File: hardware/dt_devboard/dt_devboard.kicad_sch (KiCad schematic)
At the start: 1 part

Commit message: added hieracrchial sheet structure on schematic
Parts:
- removed IC?: STM32WB35CEU6A, QFN50P700X700X60-49N-D, symbol SamacSys_Parts:STM32WB35CEU6A
- added IC?: MIMXRT1015CAF4A, QFP50P1600X1600X170-100N, symbol MIMXRT1015CAF4A:MIMXRT1015CAF4A
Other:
- added sheet Power (power_subsystem.kicad_sch)
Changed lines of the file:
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@@
 (kicad_sch (version 20211123) (generator eeschema)
-  (paper "A4")
-  (symbol (lib_id "SamacSys_Parts:STM32WB35CEU6A") (at 44.45 45.72 0) (unit 1)
+  (paper "A2")
+  (symbol (lib_id "MIMXRT1015CAF4A:MIMXRT1015CAF4A") (at 49.53 57.15 0) (unit 1)
     (in_bom yes) (on_board yes) (fields_autoplaced)
-    (property "Reference" "IC?" (id 0) (at 95.25 39.1412 0))
-    (property "Value" "STM32WB35CEU6A" (id 1) (at 95.25 41.6812 0))
-    (property "Footprint" "QFN50P700X700X60-49N-D" (id 2) (at 86.36 33.02 0)
+    (property "Reference" "IC?" (id 0) (at 130.81 50.5712 0))
+    (property "Value" "MIMXRT1015CAF4A" (id 1) (at 130.81 53.1112 0))
+    (property "Footprint" "QFP50P1600X1600X170-100N" (id 2) (at 121.92 34.29 0)
       (effects (font (size 1.27 1.27)) (justify left) hide)
     )
-    (property "Datasheet" "https://componentsearchengine.com/Datasheets/2/STM32WB35CEU6A.pdf" (id 3) (at 86.36 35.56 0)
+    (property "Datasheet" "http://www.nxp.com/docs/en/data-sheet/IMXRT1015IEC.pdf" (id 3) (at 121.92 36.83 0)
       (effects (font (size 1.27 1.27)) (justify left) hide)
     )
-    (property "Description" "ARM Microcontrollers - MCU 16/32-BITS MICROS" (id 4) (at 86.36 38.1 0)
+    (property "Description" "ARM Microcontrollers - MCU i.MXRT1015, 100LQFP" (id 4) (at 121.92 39.37 0)
       (effects (font (size 1.27 1.27)) (justify left) hide)
     )
-    (property "Height" "0.6" (id 5) (at 86.36 40.64 0)
+    (property "Height" "1.7" (id 5) (at 121.92 41.91 0)
       (effects (font (size 1.27 1.27)) (justify left) hide)
     )
-    (property "Manufacturer_Name" "STMicroelectronics" (id 6) (at 86.36 43.18 0)
+    (property "Manufacturer_Name" "NXP" (id 6) (at 121.92 44.45 0)
       (effects (font (size 1.27 1.27)) (justify left) hide)
     )
-    (property "Manufacturer_Part_Number" "STM32WB35CEU6A" (id 7) (at 86.36 45.72 0)
+    (property "Manufacturer_Part_Number" "MIMXRT1015CAF4A" (id 7) (at 121.92 46.99 0)
       (effects (font (size 1.27 1.27)) (justify left) hide)
     )
-    (property "Mouser Part Number" "511-STM32WB35CEU6A" (id 8) (at 86.36 48.26 0)
+    (property "Mouser Part Number" "771-MIMXRT1015CAF4A" (id 8) (at 121.92 49.53 0)
       (effects (font (size 1.27 1.27)) (justify left) hide)
     )
-    (property "Mouser Price/Stock" "https://www.mouser.co.uk/ProductDetail/STMicroelectronics/STM32WB35CEU6A?qs=DPoM0jnrROX%252BdiHaOx6y1Q%3D%3D" (id 9) (at 86.36 50.8 0)
+    (property "Mouser Price/Stock" "https://www.mouser.co.uk/ProductDetail/NXP-Semiconductors/MIMXRT1015CAF4A?qs=l7cgNqFNU1janL%2F6ip864Q%3D%3D" (id 9) (at 121.92 52.07 0)
       (effects (font (size 1.27 1.27)) (justify left) hide)
     )
-    (property "Arrow Part Number" "STM32WB35CEU6A" (id 10) (at 86.36 53.34 0)
+    (property "Arrow Part Number" "" (id 10) (at 121.92 54.61 0)
       (effects (font (size 1.27 1.27)) (justify left) hide)
     )
-    (property "Arrow Price/Stock" "https://www.arrow.com/en/products/stm32wb35ceu6a/stmicroelectronics?region=nac" (id 11) (at 86.36 55.88 0)
+    (property "Arrow Price/Stock" "" (id 11) (at 121.92 57.15 0)
       (effects (font (size 1.27 1.27)) (justify left) hide)
     )
     (pin "1")
     (pin "10")
+    (pin "100")
     (pin "11")
     (pin "12")
@@
     (pin "49")
     (pin "5")
+    (pin "50")
+    (pin "51")
+    (pin "52")
+    (pin "53")
+    (pin "54")
+    (pin "55")
+    (pin "56")
+    (pin "57")
+    (pin "58")
+    (pin "59")
     (pin "6")
+    (pin "60")
+    (pin "61")
+    (pin "62")
+    (pin "63")
+    (pin "64")
+    (pin "65")
+    (pin "66")
+    (pin "67")
+    (pin "68")
+    (pin "69")
     (pin "7")
+    (pin "70")
+    (pin "71")
+    (pin "72")
+    (pin "73")
+    (pin "74")
+    (pin "75")
+    (pin "76")
+    (pin "77")
+    (pin "78")
+    (pin "79")
     (pin "8")
+    (pin "80")
+    (pin "81")
+    (pin "82")
+    (pin "83")
+    (pin "84")
+    (pin "85")
+    (pin "86")
+    (pin "87")
+    (pin "88")
+    (pin "89")
     (pin "9")
+    (pin "90")
+    (pin "91")
+    (pin "92")
+    (pin "93")
+    (pin "94")
+    (pin "95")
+    (pin "96")
+    (pin "97")
+    (pin "98")
+    (pin "99")
+  )
+  (sheet (at 491.49 58.42) (size 50.8 71.12) (fields_autoplaced)
+    (stroke (width 0.1524) (type solid) (color 0 0 0 0))
+    (fill (color 0 0 0 0.0000))
+    (property "Sheet name" "Power" (id 0) (at 491.49 57.7084 0)
+      (effects (font (size 1.27 1.27)) (justify left bottom))
+    )
+    (property "Sheet file" "power_subsystem.kicad_sch" (id 1) (at 491.49 130.1246 0)
+      (effects (font (size 1.27 1.27)) (justify left top))
+    )
   )
   (sheet_instances
     (path "/" (page "1"))
+    (path "/6fe27d7a-8728-4218-b48e-6f66377c607f" (page "2"))
   )
   (symbol_instances
-    (path "/403cca15-d759-4eca-91db-c121522189fc"
-      (reference "IC?") (unit 1) (value "STM32WB35CEU6A") (footprint "QFN50P700X700X60-49N-D")
+    (path "/a108bf74-3a91-4c0a-8c67-2d89e262b919"
+      (reference "IC?") (unit 1) (value "MIMXRT1015CAF4A") (footprint "QFP50P1600X1600X170-100N")
+    )
+    (path "/6fe27d7a-8728-4218-b48e-6f66377c607f/38cad123-e6f8-46ac-bb65-7bf207c8a5a7"
+      (reference "J?") (unit 1) (value "UJ31-CH-G1-SMT-TR") (footprint "CUI_UJ31-CH-G1-SMT-TR")
     )
   )

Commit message: added USB signals to MCU
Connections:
- net USB_DN1: now reaches IC?.41 (USB_OTG1_DN)
- net USB_DP1: now reaches IC?.42 (USB_OTG1_DP)
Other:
- sheet Power ports: added USB_DN1, USB_DN2, USB_DP1, USB_DP2; removed none
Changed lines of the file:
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@@
 (kicad_sch (version 20211123) (generator eeschema)
   (paper "A2")
+  (wire (pts (xy 95.25 146.05) (xy 95.25 151.13))
+    (stroke (width 0) (type default) (color 0 0 0 0))
+  )
+  (wire (pts (xy 97.79 146.05) (xy 97.79 151.13))
+    (stroke (width 0) (type default) (color 0 0 0 0))
+  )
+  (hierarchical_label "USB_DP1" (shape input) (at 97.79 151.13 270)
+    (effects (font (size 1.27 1.27)) (justify right))
+  )
+  (hierarchical_label "USB_DN1" (shape input) (at 95.25 151.13 270)
+    (effects (font (size 1.27 1.27)) (justify right))
+  )
   (symbol (lib_id "MIMXRT1015CAF4A:MIMXRT1015CAF4A") (at 49.53 57.15 0) (unit 1)
     (in_bom yes) (on_board yes) (fields_autoplaced)
@@
       (effects (font (size 1.27 1.27)) (justify left top))
     )
+    (pin "USB_DP2" output (at 491.49 69.85 180)
+      (effects (font (size 1.27 1.27)) (justify left))
+    )
+    (pin "USB_DP1" output (at 491.49 74.93 180)
+      (effects (font (size 1.27 1.27)) (justify left))
+    )
+    (pin "USB_DN1" output (at 491.49 80.01 180)
+      (effects (font (size 1.27 1.27)) (justify left))
+    )
+    (pin "USB_DN2" output (at 491.49 85.09 180)
+      (effects (font (size 1.27 1.27)) (justify left))
+    )
   )
   (sheet_instances
@@
   )
   (symbol_instances
+    (path "/6fe27d7a-8728-4218-b48e-6f66377c607f/31cac15e-bcad-4ac1-ba6d-6a7d3365c9db"
+      (reference "#PWR?") (unit 1) (value "VBUS") (footprint "")
+    )
+    (path "/6fe27d7a-8728-4218-b48e-6f66377c607f/5a889284-4c9f-49be-8f02-e43e18550914"
+      (reference "#PWR?") (unit 1) (value "GND") (footprint "")
+    )
+    (path "/6fe27d7a-8728-4218-b48e-6f66377c607f/60b6fd94-83fa-4737-bac1-4732bb229ea8"
+      (reference "D?") (unit 1) (value "SML-D12M1WT86") (footprint "LED_SML-D12M1WT86")
+    )
     (path "/a108bf74-3a91-4c0a-8c67-2d89e262b919"
       (reference "IC?") (unit 1) (value "MIMXRT1015CAF4A") (footprint "QFP50P1600X1600X170-100N")

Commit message: added schematic sheets, symbols, and esp32 design
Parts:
- added C1: 10uF, symbol Device:C
- added C10, C11: TBD, symbol Device:C
- added C12, C13, C14, C2, C6: 0.1uF, symbol Device:C
- added C3, C5, C7, C8, C9: NC, symbol Device:C
- added C4: 1uF, symbol Device:C
- added IC2: ESP32-C3, QFN50P500X500X90-33N-D, symbol SamacSys_Parts:ESP32-C3
- added L1: TBD, symbol Device:L
- added L2: 2.0nH, symbol Device:L
- added PCBANT1: ANT1, symbol Custom:ANT1
- added R1: 0, symbol Device:R_US
- added R2: 499, symbol Device:R_US
- added Y1: Crystal_GND24, symbol Device:Crystal_GND24
- gave numbers to parts that had none: 1
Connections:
- new net: C11.2, IC2.29 (XTAL_N), Y1.3
- new net: C2.1, L1.1, PCBANT1. (LNA_OUT)
- new net: C5.1, IC2.1 (LNA_IN), L1.2
- new net: C10.2, R1.1, Y1.1
- new net: IC2.30 (XTAL_P), R1.2
- new net: C7.1, IC2.2 (VDD3P3_1), IC2.3 (VDD3P3_2), L2.2
- new net: IC2.28 (U0TXD), R2.2
- new net +3V3: C1.1, C12.1, C13.1, C14.1, C3.1, C4.1, C6.1, C8.1, C9.1, IC2.11 (VDD3P3_RTC), IC2.17 (VDD3P3_CPU), IC2.18 (VDD_SPI), IC2.31 (VDDA_1), IC2.32 (VDDA_2), L2.1
- new net CHIP_EN: IC2.7 (CHIP_EN)
- new net GND: C1.2, C10.1, C11.1, C12.2, C13.2, C14.2, C2.2, C3.2, C4.2, C5.2, C6.2, C7.2, C8.2, C9.2, IC2.33 (GND), PCBANT1. (LNA_OUT), Y1.2, Y1.4
- new net GPIO0: IC2.4 (XTAL_32K_P)
- new net GPIO1: IC2.5 (XTAL_32K_N)
- new net GPIO10: IC2.16 (GPIO10)
- new net GPIO12: IC2.19 (SPIHD)
- new net GPIO13: IC2.20 (SPIWP)
- new net GPIO18/USB_D-: IC2.25 (GPIO18)
- new net GPIO19/USB_D+: IC2.26 (GPIO19)
- new net GPIO2: IC2.6 (GPIO2)
- new net GPIO3: IC2.8 (GPIO3)
- new net GPIO8: IC2.14 (GPIO8)
- new net GPIO9: IC2.15 (GPIO9)
- new net MTDI: IC2.10 (MTDI)
- new net MTMS: IC2.9 (MTMS)
- new net SPICLK: IC2.22 (SPICLK)
- new net SPICS0: IC2.21 (SPICS0)
- new net SPID: IC2.23 (SPID)
- new net SPIQ: IC2.24 (SPIQ)
- new net U0RXD: IC2.27 (U0RXD)
- new net U0TXD: R2.1
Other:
- sheet Power renamed usb_subsystem
- added sheet external_clocks (external_clocks_sch.kicad_sch)
- added sheet external_memory (external_memory.kicad_sch)
- sheet usb_subsystem: file power_subsystem.kicad_sch -> usb_subsystem.kicad_sch
- note added: "32K crystal"
- note added: "ESP32"
- note added: "MCU"
- moved on the sheet: IC1

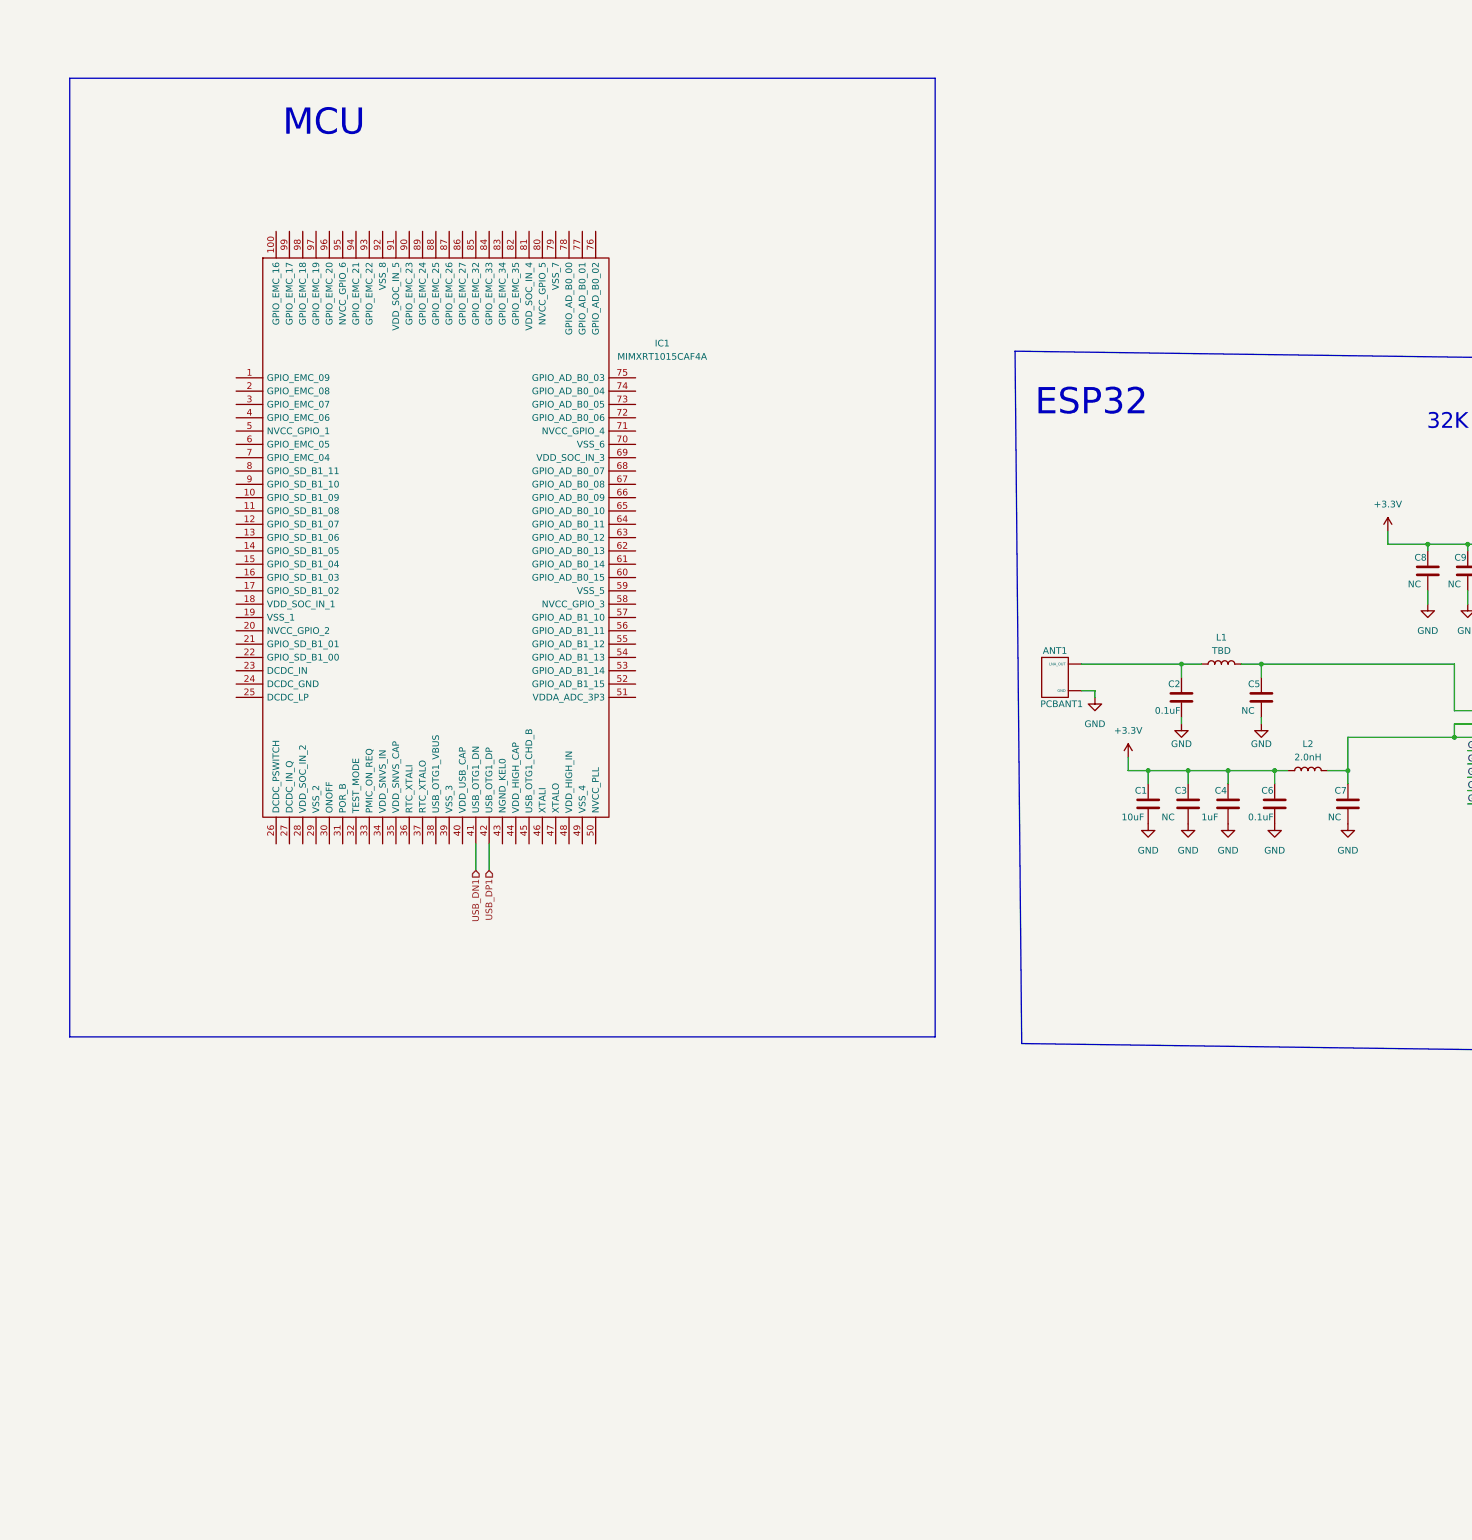
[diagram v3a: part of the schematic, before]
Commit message: added JTAG and SD connectors
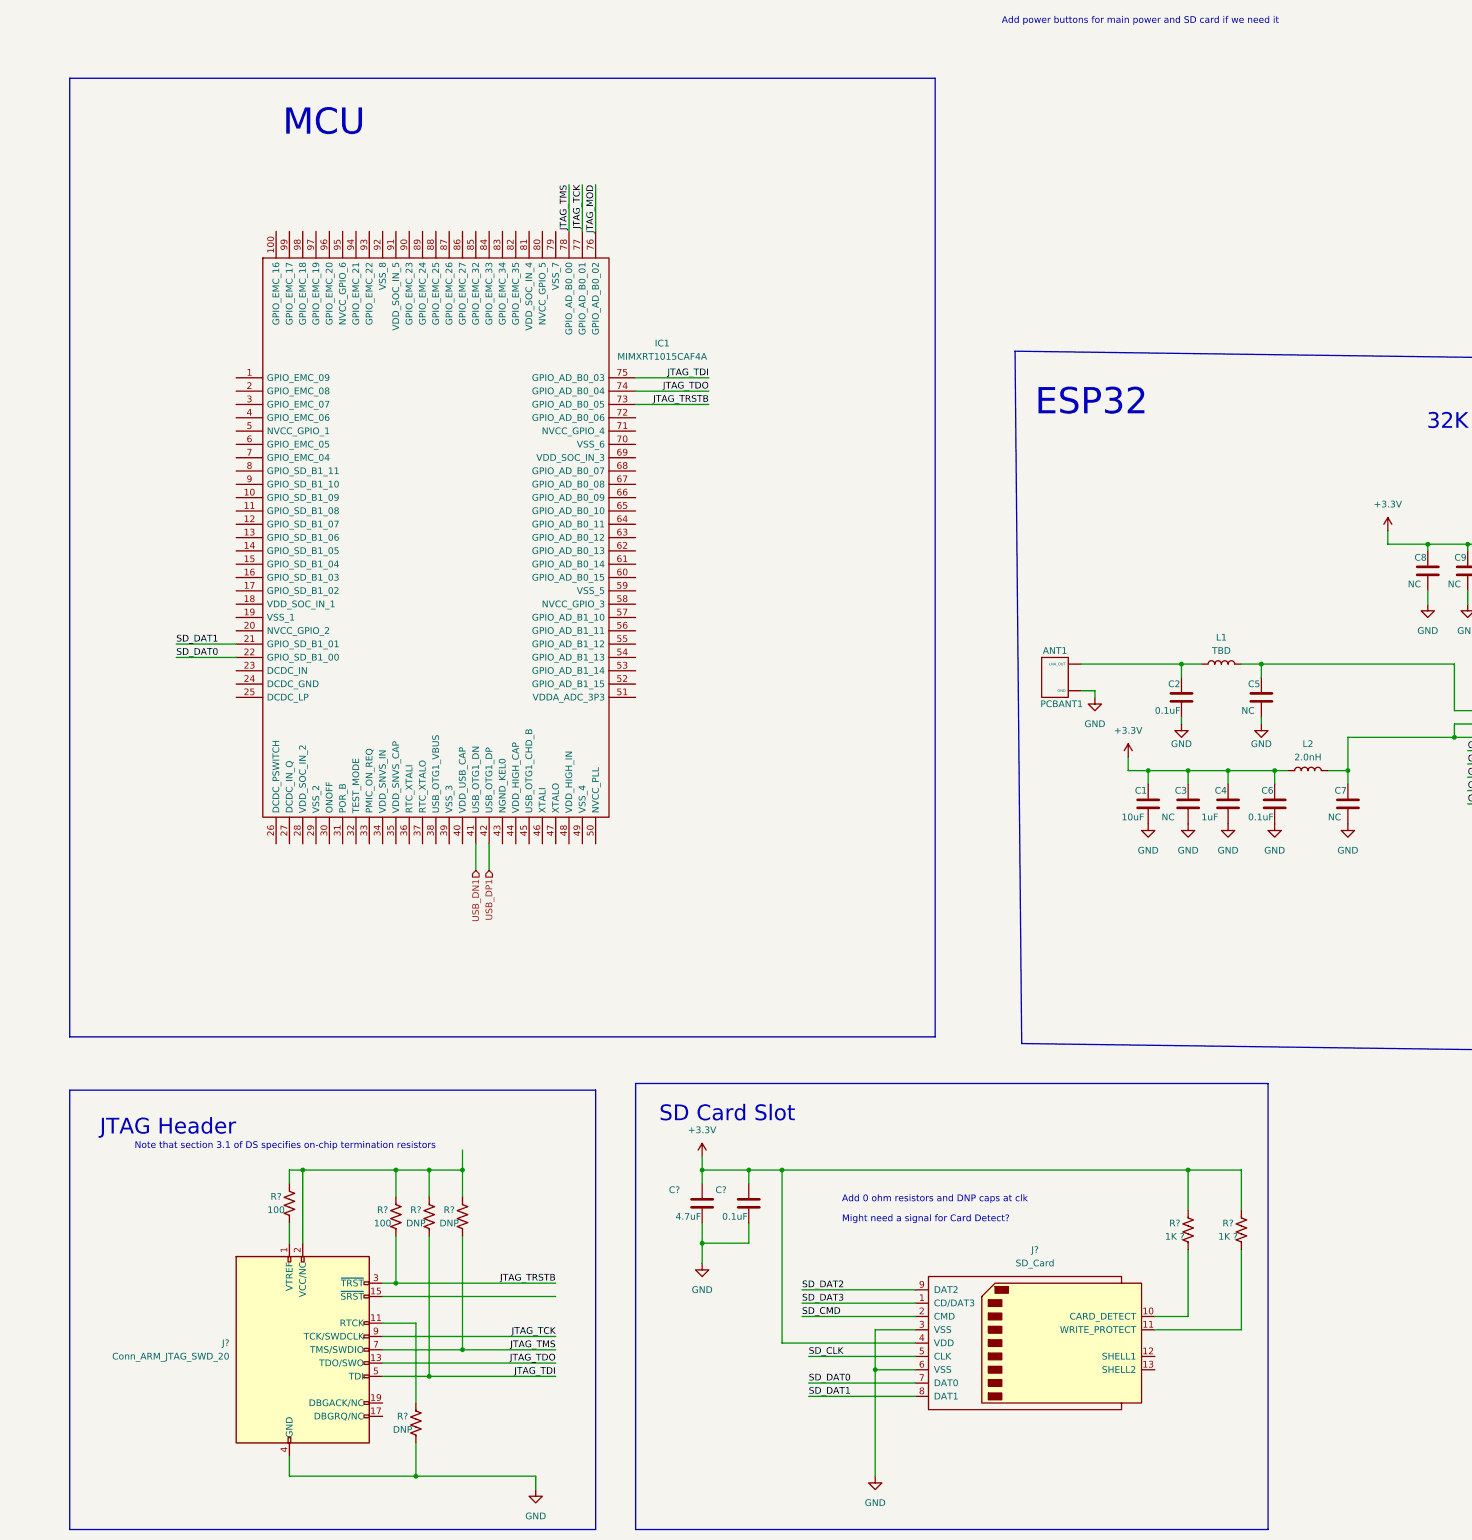
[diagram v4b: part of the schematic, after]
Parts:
- added C?: 0.1uF, symbol Device:C
- added C?: 4.7uF, symbol Device:C
- added J?: Conn_ARM_JTAG_SWD_20, symbol Connector:Conn_ARM_JTAG_SWD_20
- added J?: SD_Card, symbol Connector:SD_Card
- added R? (x2): 1K ?, symbol Device:R_US
- added R? (x3): DNP, symbol Device:R_US
- added R? (x2): 100, symbol Device:R_US
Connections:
- net +3V3: now also C?.1, C?.1, J?.4 (VDD), R?.1, R?.1
- net GND: now also C?.2, C?.2, J?.10 (GND), J?.12 (GND), J?.14 (GND), J?.16 (GND), J?.18 (GND), J?.20 (GND), J?.3 (VSS), J?.4 (GND), J?.6 (GND), J?.6 (VSS), J?.8 (GND), R?.2
- net SD_DAT1: now reaches IC1.21 (GPIO_SD_B1_01)
- net SD_DAT1: now also J?.8 (DAT1)
- net SD_DAT0: now reaches IC1.22 (GPIO_SD_B1_00)
- net SD_DAT0: now also J?.7 (DAT0)
- net JTAG_TRSTB: now reaches IC1.73 (GPIO_AD_B0_05)
- net JTAG_TRSTB: now also J?.3 (~{TRST}), R?.2
- net JTAG_TDO: now reaches IC1.74 (GPIO_AD_B0_04)
- net JTAG_TDO: now also J?.13 (TDO/SWO)
- net JTAG_TDI: now reaches IC1.75 (GPIO_AD_B0_03)
- net JTAG_TDI: now also J?.5 (TDI), R?.2
- net JTAG_MOD: now reaches IC1.76 (GPIO_AD_B0_02)
- net JTAG_TCK: now reaches IC1.77 (GPIO_AD_B0_01)
- net JTAG_TCK: now also J?.9 (TCK/SWDCLK)
- net JTAG_TMS: now reaches IC1.78 (GPIO_AD_B0_00)
- net JTAG_TMS: now also J?.7 (TMS/SWDIO), R?.2
- new net: J?.1 (VTREF), R?.2
- new net: J?.11 (RTCK), R?.1
- new net: J?.2 (VCC/NC), R?.1, R?.1, R?.1, R?.1
- new net: J?.10 (CARD_DETECT), R?.2
- new net: J?.11 (WRITE_PROTECT), R?.2
- new net SD_CLK: J?.5 (CLK)
- new net SD_CMD: J?.2 (CMD)
- new net SD_DAT2: J?.9 (DAT2)
- new net SD_DAT3: J?.1 (CD/DAT3)
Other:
- note added: "Add 0 ohm resistors and DNP caps at clk"
- note added: "Add power buttons for main power and SD card if we need it"
- note added: "JTAG Header"
- note added: "Might need a signal for Card Detect?"
- note added: "Note that section 3.1 of DS specifies on-chip termination resistors"
- note added: "SD Card Slot"
